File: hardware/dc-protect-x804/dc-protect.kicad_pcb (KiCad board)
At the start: 2 copper layers, 34 x 51 mm, 15 parts, among them P1 CON-SENSOR2-BLANK, U1 DC-Protect

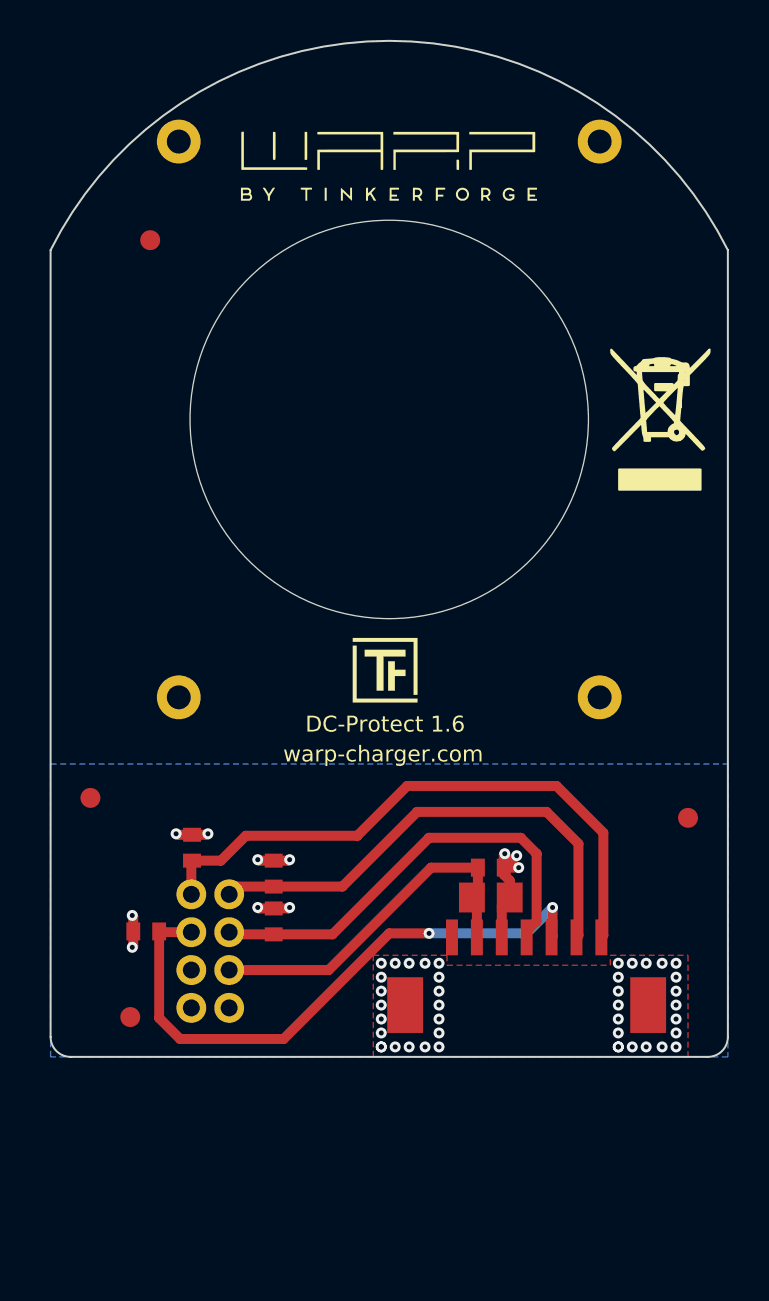
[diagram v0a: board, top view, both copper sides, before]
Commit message: Hardware: changed dc-protect-x804 pcb layout
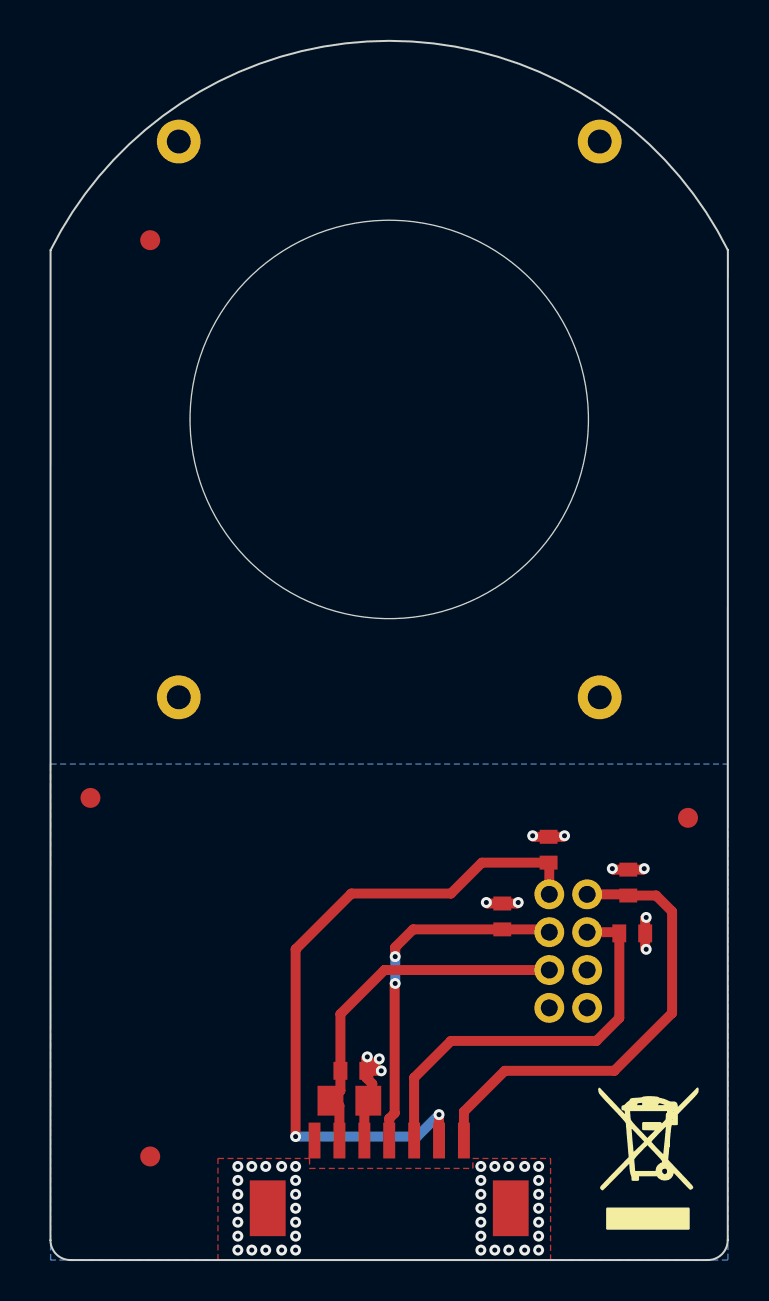
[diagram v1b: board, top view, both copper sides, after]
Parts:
- G*** (x2): moved to B.Cu
- U1: moved to F.Cu
- moved VAL 37.1 mm to (133.0, 122.1)
- moved C3 24.4 mm to (132.2, 110.8), turned to 0 degrees
- moved C1 22.0 mm to (132.0, 108.2)
- moved C2 13.9 mm to (128.0, 106.6)
- moved C5 12.4 mm to (118.0, 119.2)
- moved P1 12.3 mm to (120.0, 126.0)
- moved C6 12.3 mm to (118.2, 117.7)
- moved C4 11.5 mm to (125.7, 110.0)
- moved Fiducial_Mark 7.07 mm to (108.0, 122.0)
- moved G*** 1.30 mm to (120.0, 71.0), turned to 180 degrees
- moved G*** 0.28 mm to (120.0, 97.4), turned to 180 degrees
- turned U1 to 0 degrees
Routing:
- net Net-(C3-Pad1): track 30.4 -> 20.6 mm, vias 2 -> 0
- net Net-(C2-Pad1): track 24.7 -> 34.5 mm, vias 0 -> 2
- net Net-(C1-Pad1): track 30.2 -> 23.6 mm
- net Net-(C4-Pad1): track 22.2 -> 18.0 mm, vias 0 -> 2
- net GND: vias 53 -> 51
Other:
- board size 34 x 51 mm -> 34 x 61.2 mm

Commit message: set grid origin, move fiducials
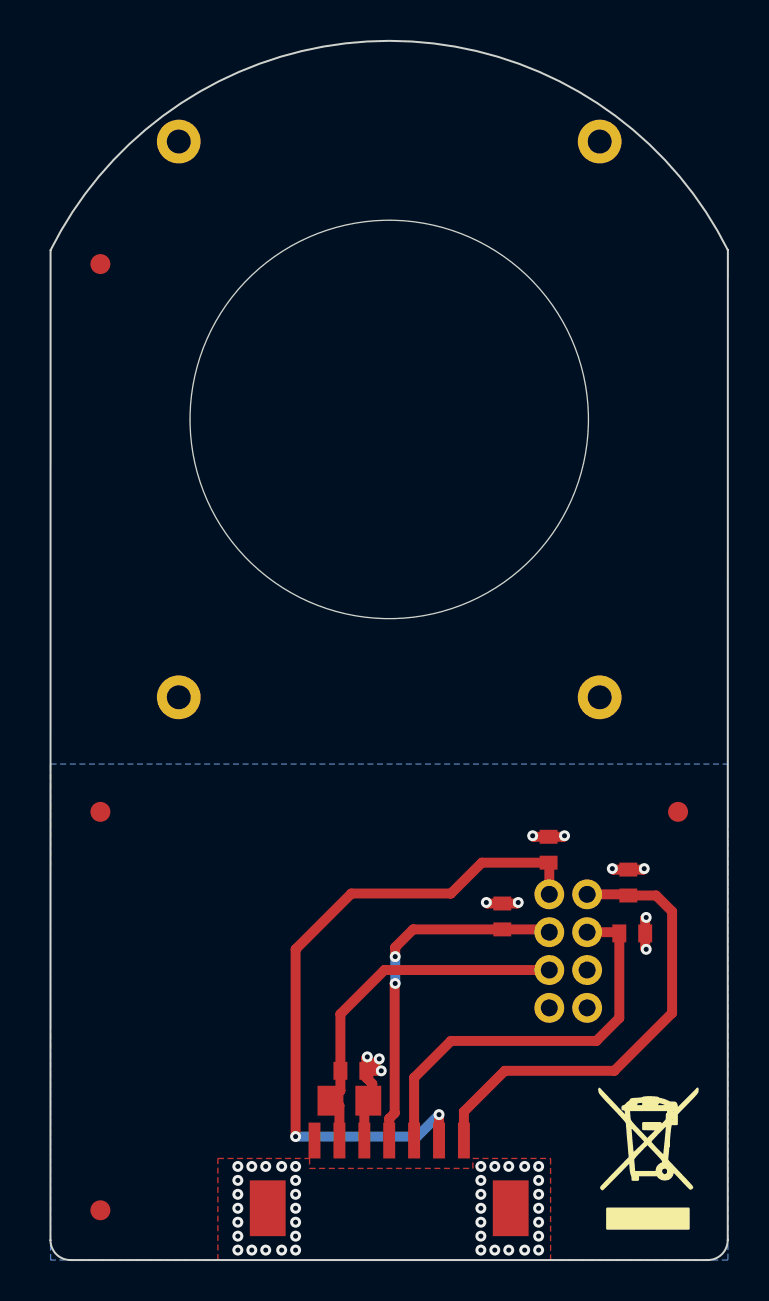
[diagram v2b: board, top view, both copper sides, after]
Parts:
- moved Fiducial_Mark 3.68 mm to (105.5, 124.7)
- moved Fiducial_Mark 2.77 mm to (105.5, 77.2)
- moved Fiducial_Mark 0.86 mm to (105.5, 104.7)
- moved Fiducial_Mark 0.58 mm to (134.5, 104.7)
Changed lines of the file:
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@@
   (setup
     (pad_to_mask_clearance 0)
-    (aux_axis_origin 120 85)
-    (grid_origin 120 85)
+    (aux_axis_origin 103 127.2)
+    (grid_origin 103 127.2)
     (pcbplotparams
       (layerselection 0x00010fc_ffffffff)
@@
   (net 9 "unconnected-(U1-Pad7)")
   (footprint "kicad-libraries:Fiducial_Mark" (layer "F.Cu")
-    (at 105 104)
+    (at 105.5 104.7)
     (attr smd)
     (fp_text reference "Fiducial_Mark" (at 0 0) (layer "F.SilkS") hide
@@
   )
   (footprint "kicad-libraries:Fiducial_Mark" (layer "F.Cu")
-    (at 135 105)
+    (at 134.5 104.7)
     (attr smd)
     (fp_text reference "Fiducial_Mark" (at 0 0) (layer "F.SilkS") hide
@@
   )
   (footprint "kicad-libraries:Fiducial_Mark" (layer "F.Cu")
-    (at 108 122)
+    (at 105.5 124.7)
     (attr smd)
     (fp_text reference "Fiducial_Mark" (at 0 0) (layer "F.SilkS") hide
@@
   )
   (footprint "kicad-libraries:Fiducial_Mark" (layer "F.Cu")
-    (at 108 76)
+    (at 105.5 77.2)
     (attr smd)
     (fp_text reference "Fiducial_Mark" (at 0 0) (layer "F.SilkS") hide

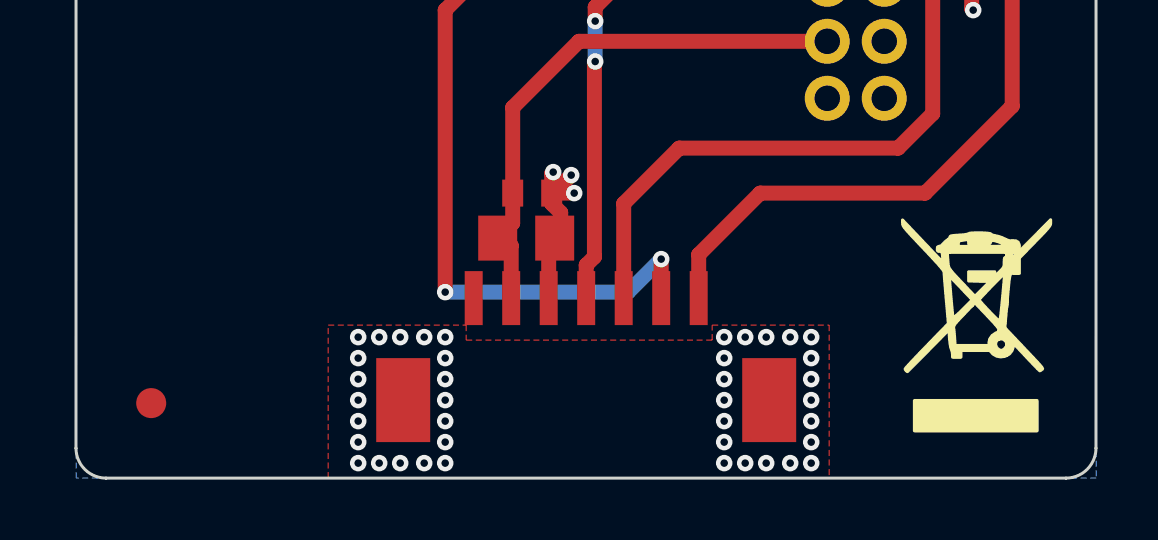
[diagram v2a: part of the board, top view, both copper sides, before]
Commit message: added warp3 bohrschablone
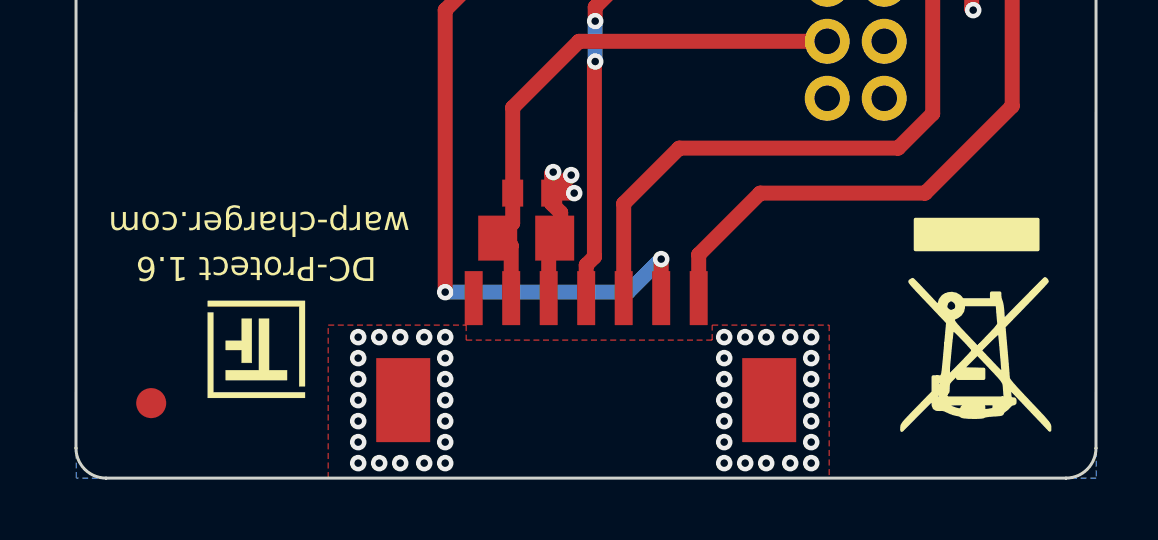
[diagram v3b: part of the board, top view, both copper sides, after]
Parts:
- removed the G*** at (120.0, 71.0)
- added G***: LOGO, kicad-libraries:LogoWARP_25x6, B.Cu at (120.0, 123.0)
- G***: moved to F.Cu
- moved G*** 27.8 mm to (109.0, 122.9)
- turned VAL to 180 degrees
